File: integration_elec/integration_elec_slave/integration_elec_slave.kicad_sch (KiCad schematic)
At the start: 0 parts

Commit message: EM - Ajout des schématiques XBEE, pas implémenté les footprints encore
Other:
- added sheet MCU (MCU.kicad_sch)
- added sheet XBEE (XBEE.kicad_sch)
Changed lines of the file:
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@@
 	(generator_version "9.0")
 	(paper "A4")
+	(sheet
+		(at 46.355 57.15)
+		(size 99.06 42.545)
+		(exclude_from_sim no)
+		(in_bom yes)
+		(on_board yes)
+		(dnp no)
+		(fields_autoplaced yes)
+		(stroke
+			(width 0.1524)
+			(type solid)
+		)
+		(fill
+			(color 0 0 0 0.0000)
+		)
+		(property "Sheetname" "XBEE"
+			(at 46.355 56.4384 0)
+			(effects
+				(font
+					(size 1.27 1.27)
+				)
+				(justify left bottom)
+			)
+		)
+		(property "Sheetfile" "XBEE.kicad_sch"
+			(at 46.355 100.2796 0)
+			(effects
+				(font
+					(size 1.27 1.27)
+				)
+				(justify left top)
+			)
+		)
+		(instances
+			(project "integration_elec_slave"
+				(path "/f8f45849-17b1-4cdb-b0ac-47b1208e44f3"
+					(page "2")
+				)
+			)
+		)
+	)
+	(sheet
+		(at 45.085 120.015)
+		(size 93.98 36.195)
+		(exclude_from_sim no)
+		(in_bom yes)
+		(on_board yes)
+		(dnp no)
+		(fields_autoplaced yes)
+		(stroke
+			(width 0.1524)
+			(type solid)
+		)
+		(fill
+			(color 0 0 0 0.0000)
+		)
+		(property "Sheetname" "MCU"
+			(at 45.085 119.3034 0)
+			(effects
+				(font
+					(size 1.27 1.27)
+				)
+				(justify left bottom)
+			)
+		)
+		(property "Sheetfile" "MCU.kicad_sch"
+			(at 45.085 156.7946 0)
+			(effects
+				(font
+					(size 1.27 1.27)
+				)
+				(justify left top)
+			)
+		)
+		(instances
+			(project "integration_elec_slave"
+				(path "/f8f45849-17b1-4cdb-b0ac-47b1208e44f3"
+					(page "3")
+				)
+			)
+		)
+	)
 	(sheet_instances
 		(path "/"

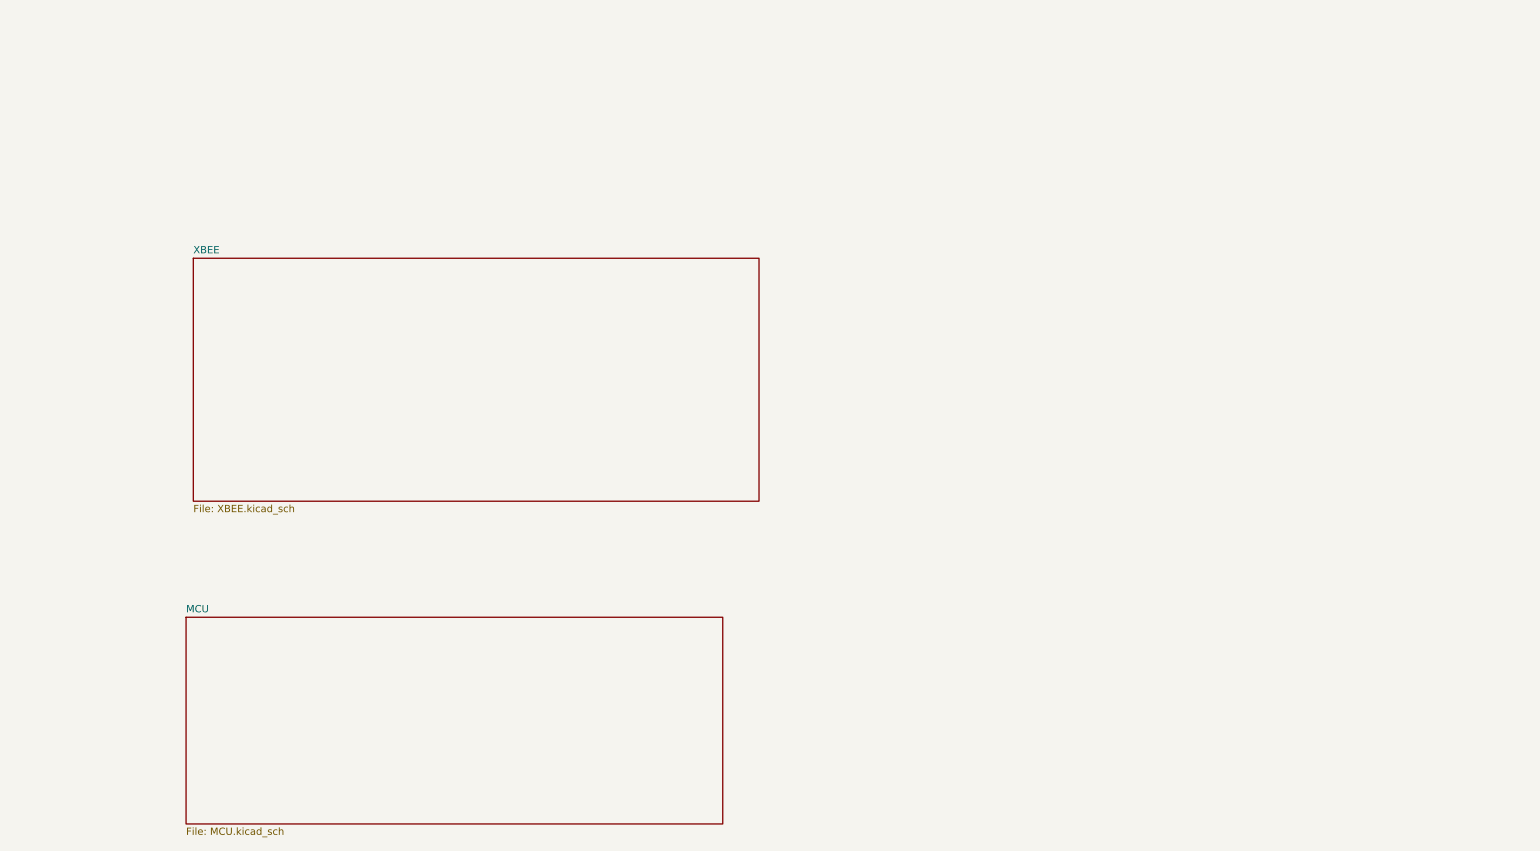
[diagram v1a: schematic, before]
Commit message: EM - Ajout des pages hiérarchiques pour le slave, next up : Master
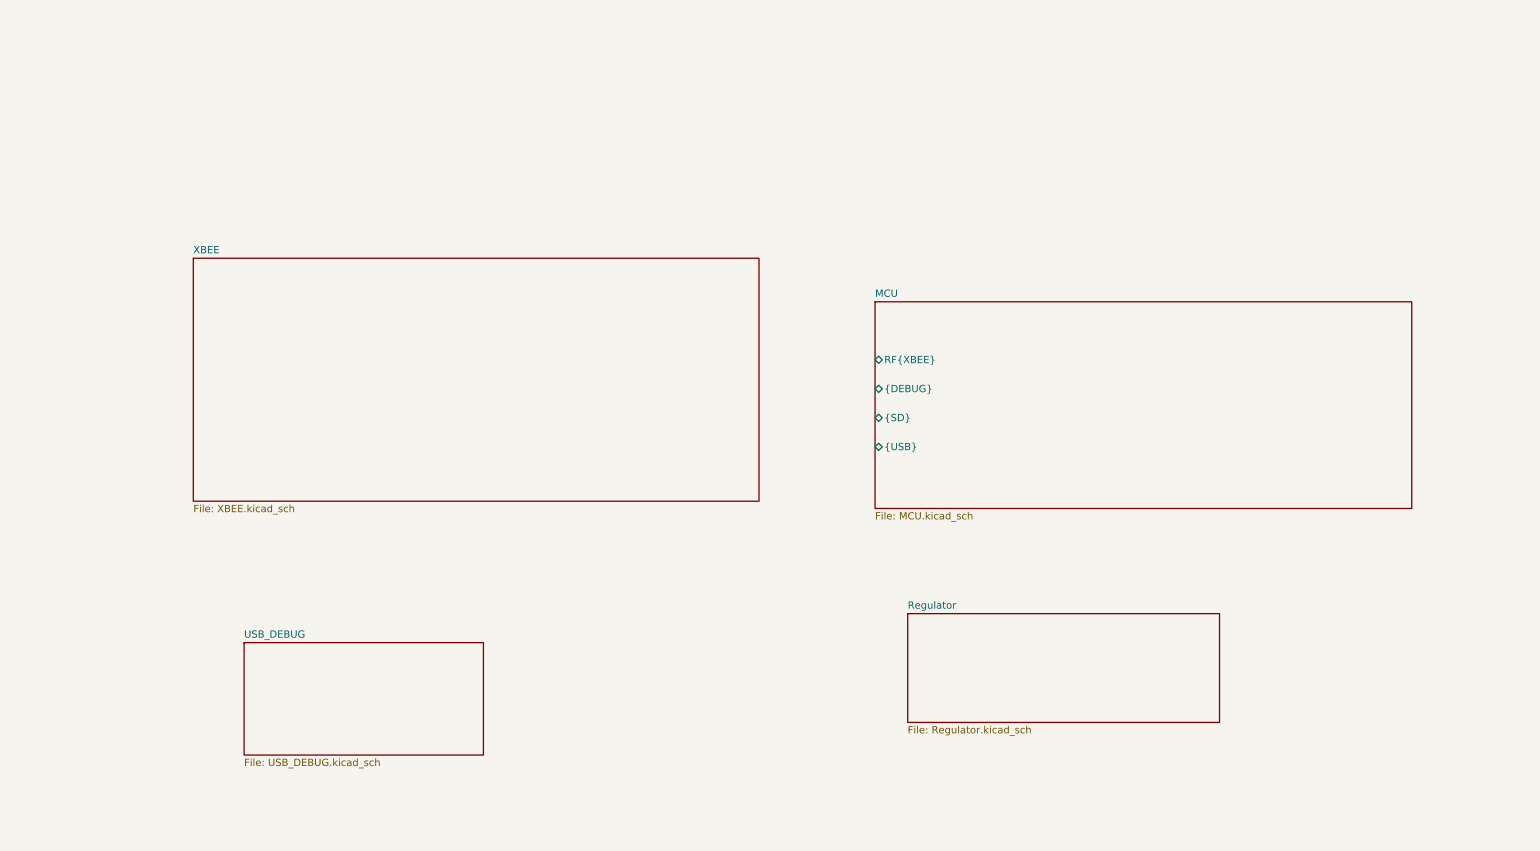
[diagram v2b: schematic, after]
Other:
- added sheet Regulator (Regulator.kicad_sch)
- added sheet USB_DEBUG (USB_DEBUG.kicad_sch)
- sheet MCU ports: added RF{XBEE}, {DEBUG}, {SD}, {USB}; removed none
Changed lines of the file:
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@@
 	(paper "A4")
+	(sheet
+		(at 171.45 119.38)
+		(size 54.61 19.05)
+		(exclude_from_sim no)
+		(in_bom yes)
+		(on_board yes)
+		(dnp no)
+		(fields_autoplaced yes)
+		(stroke
+			(width 0.1524)
+			(type solid)
+		)
+		(fill
+			(color 0 0 0 0.0000)
+		)
+		(property "Sheetname" "Regulator"
+			(at 171.45 118.6684 0)
+			(effects
+				(font
+					(size 1.27 1.27)
+				)
+				(justify left bottom)
+			)
+		)
+		(property "Sheetfile" "Regulator.kicad_sch"
+			(at 171.45 139.0146 0)
+			(effects
+				(font
+					(size 1.27 1.27)
+				)
+				(justify left top)
+			)
+		)
+		(instances
+			(project "integration_elec_slave"
+				(path "/f8f45849-17b1-4cdb-b0ac-47b1208e44f3"
+					(page "5")
+				)
+			)
+		)
+	)
 	(sheet
 		(at 46.355 57.15)
@@
 	)
 	(sheet
-		(at 45.085 120.015)
+		(at 165.735 64.77)
 		(size 93.98 36.195)
 		(exclude_from_sim no)
@@
 		)
 		(property "Sheetname" "MCU"
-			(at 45.085 119.3034 0)
+			(at 165.735 64.0584 0)
 			(effects
 				(font
@@
 		)
 		(property "Sheetfile" "MCU.kicad_sch"
-			(at 45.085 156.7946 0)
+			(at 165.735 101.5496 0)
+			(effects
+				(font
+					(size 1.27 1.27)
+				)
+				(justify left top)
+			)
+		)
+		(pin "RF{XBEE}" bidirectional
+			(at 165.735 74.93 180)
+			(effects
+				(font
+					(size 1.27 1.27)
+				)
+				(justify left)
+			)
+		)
+		(pin "{DEBUG}" bidirectional
+			(at 165.735 80.01 180)
+			(effects
+				(font
+					(size 1.27 1.27)
+				)
+				(justify left)
+			)
+		)
+		(pin "{SD}" bidirectional
+			(at 165.735 85.09 180)
+			(effects
+				(font
+					(size 1.27 1.27)
+				)
+				(justify left)
+			)
+		)
+		(pin "{USB}" bidirectional
+			(at 165.735 90.17 180)
+			(effects
+				(font
+					(size 1.27 1.27)
+				)
+				(justify left)
+			)
+		)
+		(instances
+			(project "integration_elec_slave"
+				(path "/f8f45849-17b1-4cdb-b0ac-47b1208e44f3"
+					(page "3")
+				)
+			)
+		)
+	)
+	(sheet
+		(at 55.245 124.46)
+		(size 41.91 19.685)
+		(exclude_from_sim no)
+		(in_bom yes)
+		(on_board yes)
+		(dnp no)
+		(fields_autoplaced yes)
+		(stroke
+			(width 0.1524)
+			(type solid)
+		)
+		(fill
+			(color 0 0 0 0.0000)
+		)
+		(property "Sheetname" "USB_DEBUG"
+			(at 55.245 123.7484 0)
+			(effects
+				(font
+					(size 1.27 1.27)
+				)
+				(justify left bottom)
+			)
+		)
+		(property "Sheetfile" "USB_DEBUG.kicad_sch"
+			(at 55.245 144.7296 0)
 			(effects
 				(font
@@
 			(project "integration_elec_slave"
 				(path "/f8f45849-17b1-4cdb-b0ac-47b1208e44f3"
-					(page "3")
+					(page "4")
 				)
 			)

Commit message: EM - Avancement du slave et determination ADC pour LTF6800
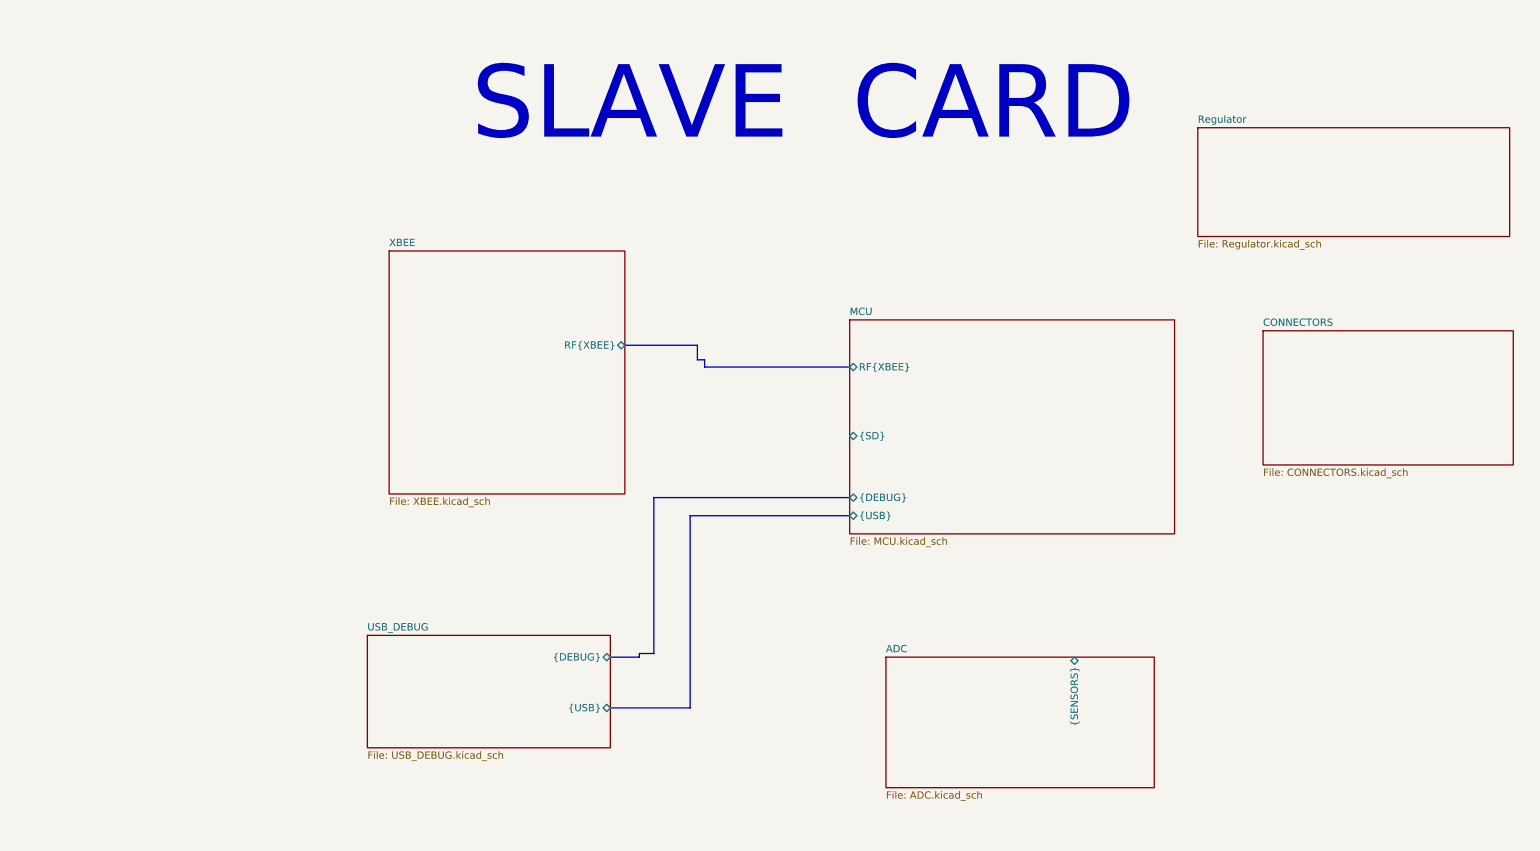
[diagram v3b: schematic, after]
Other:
- added sheet ADC (ADC.kicad_sch)
- added sheet CONNECTORS (CONNECTORS.kicad_sch)
- sheet USB_DEBUG ports: added {DEBUG}, {USB}; removed none
- sheet XBEE ports: added RF{XBEE}; removed none
- note added: "SLAVE CARD"

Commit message: EM - fuck it we merge et on cree deux branches
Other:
- sheet ADC ports: added {I2C_BUS}, {INTERRUPTS}; removed none
- sheet CONNECTORS ports: added {SENSORS}; removed none
- sheet MCU ports: added {I2C_BUS}, {INTERRUPTS}; removed {SD}
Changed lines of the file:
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@@
+	(bus
+		(pts
+			(xy 182.88 105.41) (xy 182.88 127)
+		)
+		(stroke
+			(width 0)
+			(type default)
+		)
+	)
+	(bus
+		(pts
+			(xy 242.57 119.38) (xy 242.57 91.44)
+		)
+		(stroke
+			(width 0)
+			(type default)
+		)
+	)
 	(bus
 		(pts
@@
 	(bus
 		(pts
-			(xy 124.46 126.365) (xy 127 126.365)
-		)
-		(stroke
-			(width 0)
-			(type default)
-		)
-	)
-	(bus
-		(pts
-			(xy 134.62 74.93) (xy 134.62 72.39)
-		)
-		(stroke
-			(width 0)
-			(type default)
-		)
-	)
-	(bus
-		(pts
-			(xy 124.46 127) (xy 119.38 127)
-		)
-		(stroke
-			(width 0)
-			(type default)
-		)
-	)
-	(bus
-		(pts
-			(xy 135.89 74.93) (xy 134.62 74.93)
+			(xy 194.31 105.41) (xy 194.31 127)
+		)
+		(stroke
+			(width 0)
+			(type default)
+		)
+	)
+	(bus
+		(pts
+			(xy 119.38 127) (xy 127 127)
 		)
 		(stroke
@@
 	(bus
 		(pts
-			(xy 134.62 72.39) (xy 121.92 72.39)
-		)
-		(stroke
-			(width 0)
-			(type default)
-		)
-	)
-	(bus
-		(pts
-			(xy 135.89 76.2) (xy 161.29 76.2)
-		)
-		(stroke
-			(width 0)
-			(type default)
-		)
-	)
-	(bus
-		(pts
-			(xy 135.89 74.93) (xy 135.89 76.2)
+			(xy 121.92 76.2) (xy 161.29 76.2)
+		)
+		(stroke
+			(width 0)
+			(type default)
+		)
+	)
+	(bus
+		(pts
+			(xy 200.66 119.38) (xy 242.57 119.38)
+		)
+		(stroke
+			(width 0)
+			(type default)
+		)
+	)
+	(bus
+		(pts
+			(xy 200.66 127) (xy 200.66 119.38)
 		)
 		(stroke
@@
 	(bus
 		(pts
-			(xy 124.46 126.365) (xy 124.46 127)
-		)
-		(stroke
-			(width 0)
-			(type default)
-		)
-	)
-	(bus
-		(pts
-			(xy 127 99.06) (xy 127 126.365)
+			(xy 127 99.06) (xy 127 127)
 		)
 		(stroke
@@
 	(sheet
 		(at 233.68 69.85)
-		(size 43.815 23.495)
+		(size 43.815 21.59)
 		(exclude_from_sim no)
 		(in_bom yes)
@@
 		)
 		(property "Sheetname" "CONNECTORS"
-			(at 233.68 69.1384 0)
+			(at 232.9684 91.44 90)
 			(effects
 				(font
@@
 		)
 		(property "Sheetfile" "CONNECTORS.kicad_sch"
-			(at 233.68 93.9296 0)
-			(effects
-				(font
-					(size 1.27 1.27)
-				)
-				(justify left top)
+			(at 278.0796 91.44 90)
+			(effects
+				(font
+					(size 1.27 1.27)
+				)
+				(justify left top)
+			)
+		)
+		(pin "{SENSORS}" bidirectional
+			(at 242.57 91.44 270)
+			(effects
+				(font
+					(size 1.27 1.27)
+				)
+				(justify left)
 			)
 		)
@@
 			)
 		)
+		(pin "{I2C_BUS}" bidirectional
+			(at 194.31 127 90)
+			(effects
+				(font
+					(size 1.27 1.27)
+				)
+				(justify right)
+			)
+		)
+		(pin "{INTERRUPTS}" output
+			(at 182.88 127 90)
+			(effects
+				(font
+					(size 1.27 1.27)
+				)
+				(justify right)
+			)
+		)
 		(instances
 			(project "integration_elec_slave"
@@
 	)
 	(sheet
-		(at 80.645 55.88)
+		(at 80.645 59.69)
 		(size 41.275 42.545)
 		(exclude_from_sim no)
@@
 		)
 		(property "Sheetname" "XBEE"
-			(at 80.645 55.1684 0)
+			(at 80.645 58.9784 0)
 			(effects
 				(font
@@
 		)
 		(property "Sheetfile" "XBEE.kicad_sch"
-			(at 80.645 99.0096 0)
+			(at 80.645 102.8196 0)
 			(effects
 				(font
@@
 		)
 		(pin "RF{XBEE}" bidirectional
-			(at 121.92 72.39 0)
+			(at 121.92 76.2 0)
 			(effects
 				(font
@@
 			)
 		)
-		(pin "{SD}" bidirectional
-			(at 161.29 88.265 180)
-			(effects
-				(font
-					(size 1.27 1.27)
-				)
-				(justify left)
-			)
-		)
 		(pin "{USB}" bidirectional
 			(at 161.29 102.235 180)
 			(effects
 				(font
+					(size 1.27 1.27)
+				)
+				(justify left)
+			)
+		)
+		(pin "{I2C_BUS}" bidirectional
+			(at 194.31 105.41 270)
+			(effects
+				(font
+					(size 1.27 1.27)
+				)
+				(justify left)
+			)
+		)
+		(pin "{INTERRUPTS}" output
+			(at 182.88 105.41 270)
+			(effects
+				(font

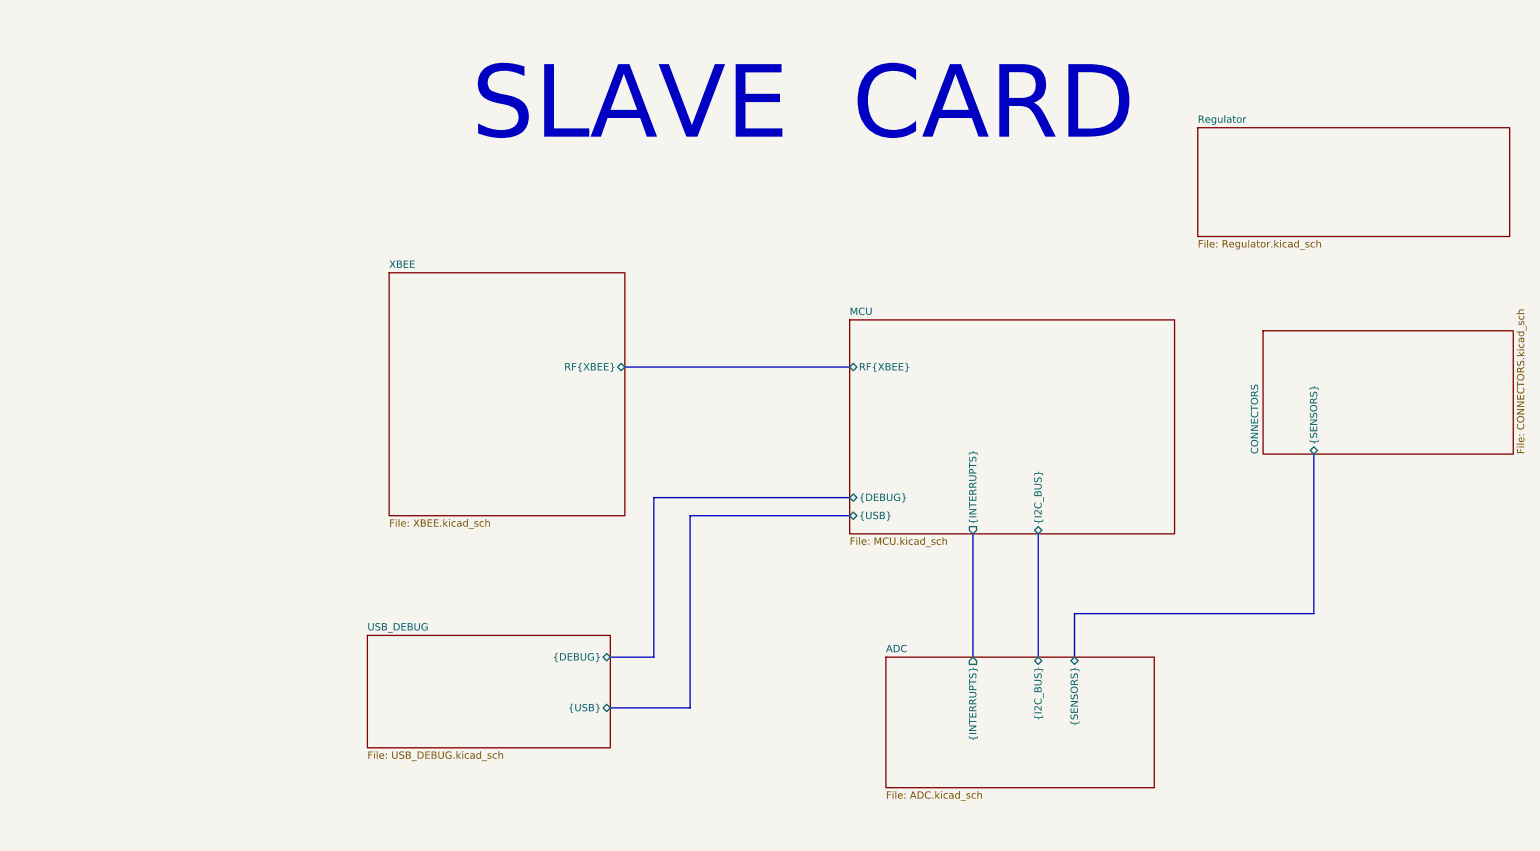
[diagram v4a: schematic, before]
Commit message: EM - Correction des bus
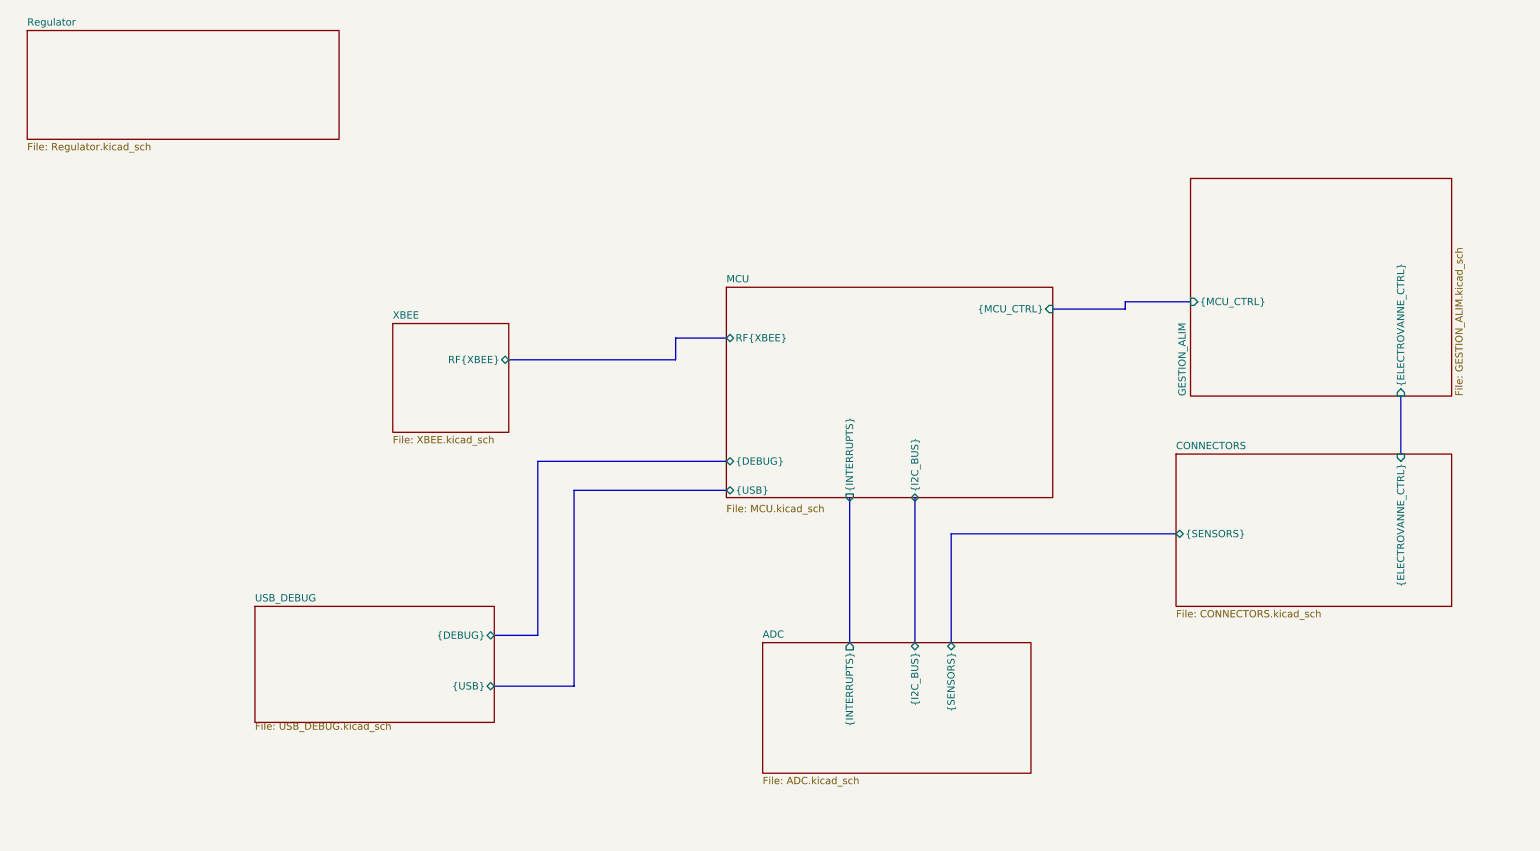
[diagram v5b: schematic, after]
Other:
- added sheet GESTION_ALIM (GESTION_ALIM.kicad_sch)
- sheet CONNECTORS ports: added {ELECTROVANNE_CTRL}; removed none
- sheet MCU ports: added {MCU_CTRL}; removed none
- note removed: "SLAVE CARD"
